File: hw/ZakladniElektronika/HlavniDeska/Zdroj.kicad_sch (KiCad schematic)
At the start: 28 parts, among them Q10 Q_PMOS_DGS-L, SW1 ON, U17 BateriCell_2x, U7 SL8261D-G3JE

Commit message: AHS-V1
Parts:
- Q10, Q? (x2), U7: JLCPCB_CORRECTION (none) -> 0;0;180
- Q? (x3): JLCPCB_CORRECTION (none) -> 0;0;-90
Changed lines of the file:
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@@
       (effects (font (size 1.27 1.27)) hide)
     )
-    (property "JLCPCB_CORRECTION" "" (at 190.5 88.9 0)
+    (property "JLCPCB_CORRECTION" "0;0;-90" (at 190.5 88.9 0)
       (effects (font (size 1.27 1.27)) hide)
     )
@@
       (effects (font (size 1.27 1.27)) hide)
     )
-    (property "JLCPCB_CORRECTION" "" (at 91.44 129.54 0)
+    (property "JLCPCB_CORRECTION" "0;0;180" (at 91.44 129.54 0)
       (effects (font (size 1.27 1.27)) hide)
     )
@@
       (effects (font (size 1.27 1.27)) hide)
     )
-    (property "JLCPCB_CORRECTION" "" (at 142.24 129.54 0)
+    (property "JLCPCB_CORRECTION" "0;0;180" (at 142.24 129.54 0)
       (effects (font (size 1.27 1.27)) hide)
     )
@@
       (effects (font (size 1.27 1.27)) hide)
     )
-    (property "JLCPCB_CORRECTION" "" (at 109.22 88.9 0)
+    (property "JLCPCB_CORRECTION" "0;0;-90" (at 109.22 88.9 0)
       (effects (font (size 1.27 1.27)) hide)
     )
@@
     )
     (property "LCSC" "C5186027" (at 179.07 58.42 0)
+      (effects (font (size 1.27 1.27)) hide)
+    )
+    (property "JLCPCB_CORRECTION" "0;0;180" (at 179.07 73.66 0)
       (effects (font (size 1.27 1.27)) hide)
     )
@@
       (effects (font (size 1.27 1.27)) hide)
     )
-    (property "JLCPCB_CORRECTION" "" (at 157.48 66.04 0)
+    (property "JLCPCB_CORRECTION" "0;0;180" (at 157.48 66.04 0)
       (effects (font (size 1.27 1.27)) hide)
     )
@@
       (effects (font (size 1.27 1.27)) hide)
     )
-    (property "JLCPCB_CORRECTION" "" (at 208.28 88.9 0)
-      (effects (font (size 1.27 1.27)) hide)
-    )
+    (property "JLCPCB_CORRECTION" "0;0;-90" (at 208.28 88.9 0)
+      (effects (font (size 1.27 1.27)) hide)
+    )

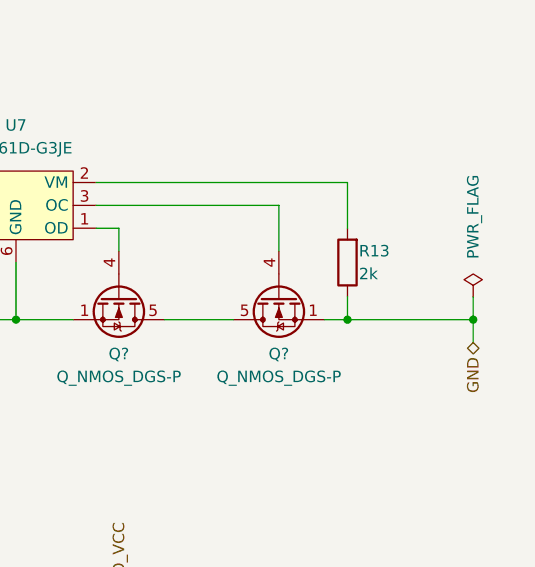
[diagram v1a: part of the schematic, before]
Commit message: Řešení issue "Držák baterek" a " SemiSemafor V0"
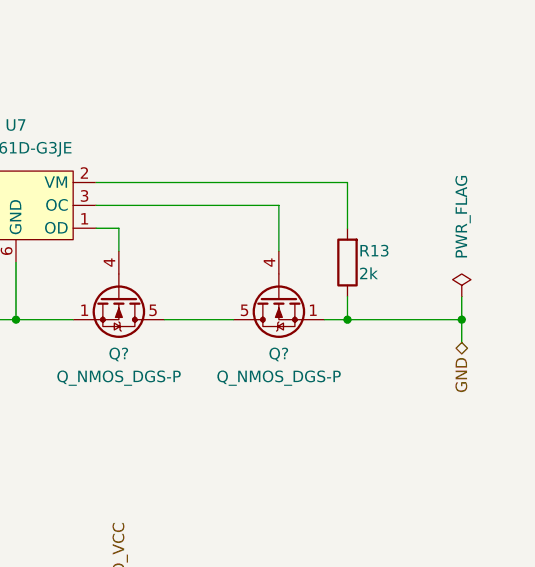
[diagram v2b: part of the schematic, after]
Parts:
- U17: footprint RKL-Batteries:battery_dock -> RKL-Batteries:2x18650-holder-jlc_SMD-typ; JLCPCB_IGNORE ignore -> (none); LCSC (none) -> C6937126
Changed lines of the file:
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@@
   (junction (at 88.9 88.9) (diameter 0) (color 0 0 0 0)
   )
-  (junction (at 229.87 88.9) (diameter 0) (color 0 0 0 0)
+  (junction (at 228.6 88.9) (diameter 0) (color 0 0 0 0)
   )
   (junction (at 160.02 50.8) (diameter 0) (color 0 0 0 0)
@@
     (stroke (width 0) (type default))
   )
-  (wire (pts (xy 215.9 88.9) (xy 229.87 88.9))
-    (stroke (width 0) (type default))
-  )
   (wire (pts (xy 203.2 88.9) (xy 195.58 88.9))
     (stroke (width 0) (type default))
@@
     (stroke (width 0) (type default))
   )
-  (wire (pts (xy 215.9 88.9) (xy 213.36 88.9))
+  (wire (pts (xy 213.36 88.9) (xy 215.9 88.9))
     (stroke (width 0) (type default))
   )
@@
     (stroke (width 0) (type default))
   )
-  (wire (pts (xy 229.87 86.36) (xy 229.87 88.9))
+  (wire (pts (xy 228.6 86.36) (xy 228.6 88.9))
     (stroke (width 0) (type default))
   )
@@
     (stroke (width 0) (type default))
   )
-  (wire (pts (xy 229.87 91.44) (xy 229.87 88.9))
+  (wire (pts (xy 228.6 91.44) (xy 228.6 88.9))
     (stroke (width 0) (type default))
   )
@@
   )
   (wire (pts (xy 88.9 139.7) (xy 88.9 134.62))
+    (stroke (width 0) (type default))
+  )
+  (wire (pts (xy 215.9 88.9) (xy 228.6 88.9))
     (stroke (width 0) (type default))
   )
@@
     (effects (font (size 1.27 1.27)) (justify left bottom))
   )
-  (hierarchical_label "GND" (shape bidirectional) (at 229.87 91.44 270) (fields_autoplaced)
+  (hierarchical_label "GND" (shape bidirectional) (at 228.6 91.44 270) (fields_autoplaced)
     (effects (font (size 1.27 1.27)) (justify right))
   )
@@
     )
   )
-  (symbol (lib_id "power:PWR_FLAG") (at 229.87 86.36 0) (unit 1)
-    (in_bom yes) (on_board yes) (dnp no)
-    (property "Reference" "#FLG02" (at 229.87 84.455 0)
-      (effects (font (size 1.27 1.27)) hide)
-    )
-    (property "Value" "PWR_FLAG" (at 229.87 77.47 90)
+  (symbol (lib_id "power:PWR_FLAG") (at 228.6 86.36 0) (unit 1)
+    (in_bom yes) (on_board yes) (dnp no)
+    (property "Reference" "#FLG02" (at 228.6 84.455 0)
+      (effects (font (size 1.27 1.27)) hide)
+    )
+    (property "Value" "PWR_FLAG" (at 228.6 77.47 90)
       (effects (font (size 1.27 1.27)))
     )
-    (property "Footprint" "" (at 229.87 86.36 0)
-      (effects (font (size 1.27 1.27)) hide)
-    )
-    (property "Datasheet" "~" (at 229.87 86.36 0)
+    (property "Footprint" "" (at 228.6 86.36 0)
+      (effects (font (size 1.27 1.27)) hide)
+    )
+    (property "Datasheet" "~" (at 228.6 86.36 0)
       (effects (font (size 1.27 1.27)) hide)
     )
@@
       (effects (font (size 1.27 1.27)) (justify left))
     )
-    (property "Footprint" "RKL-Batteries:battery_dock" (at 86.36 80.01 0)
-      (effects (font (size 1.27 1.27)) hide)
-    )
-    (property "Datasheet" "" (at 86.36 80.01 0)
-      (effects (font (size 1.27 1.27)) hide)
-    )
-    (property "JLCPCB_IGNORE" "ignore" (at 86.36 80.01 0)
-      (effects (font (size 1.27 1.27)) hide)
-    )
+    (property "Footprint" "RKL-Batteries:2x18650-holder-jlc_SMD-typ" (at 86.36 80.01 0)
+      (effects (font (size 1.27 1.27)) hide)
+    )
+    (property "Datasheet" "https://wmsc.lcsc.com/wmsc/upload/file/pdf/v2/lcsc/2306250925_MYOUNG-BH-18650-B1BA007_C6937126.pdf" (at 86.36 80.01 0)
+      (effects (font (size 1.27 1.27)) hide)
+    )
+    (property "LCSC" "C6937126" (at 86.36 80.01 0)
+      (effects (font (size 1.27 1.27)) hide)
+    )

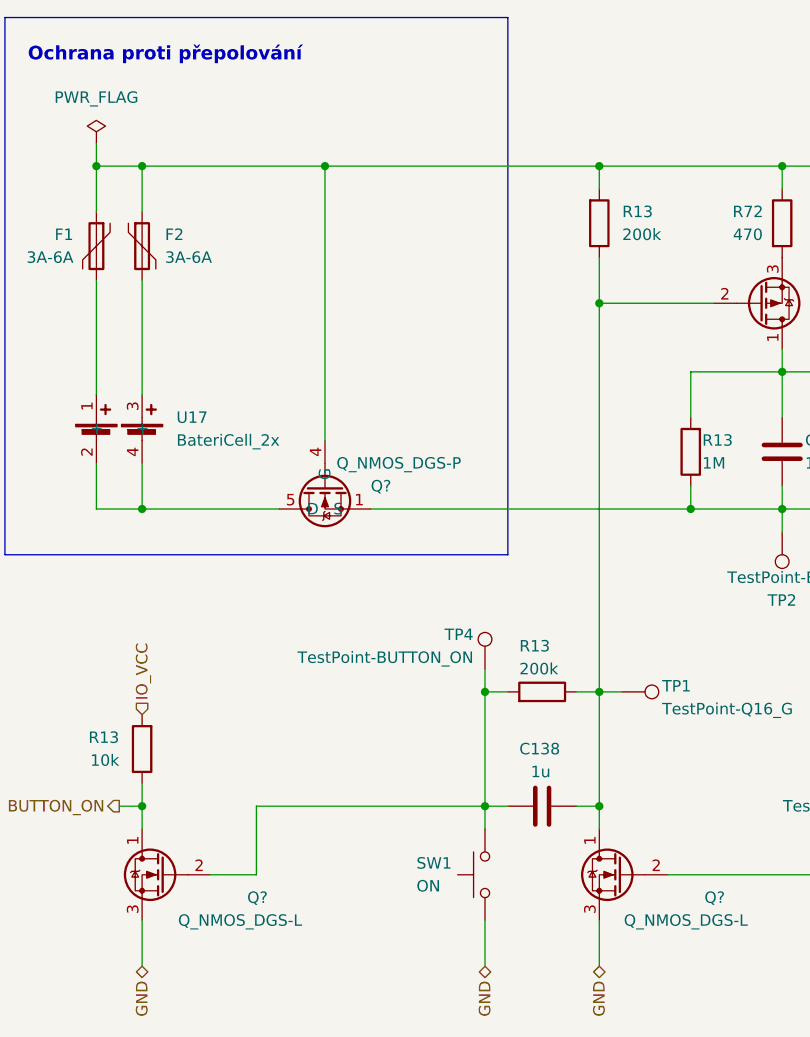
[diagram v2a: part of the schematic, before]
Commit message: Řešení issue "Čtení zapínacího tlačítka"
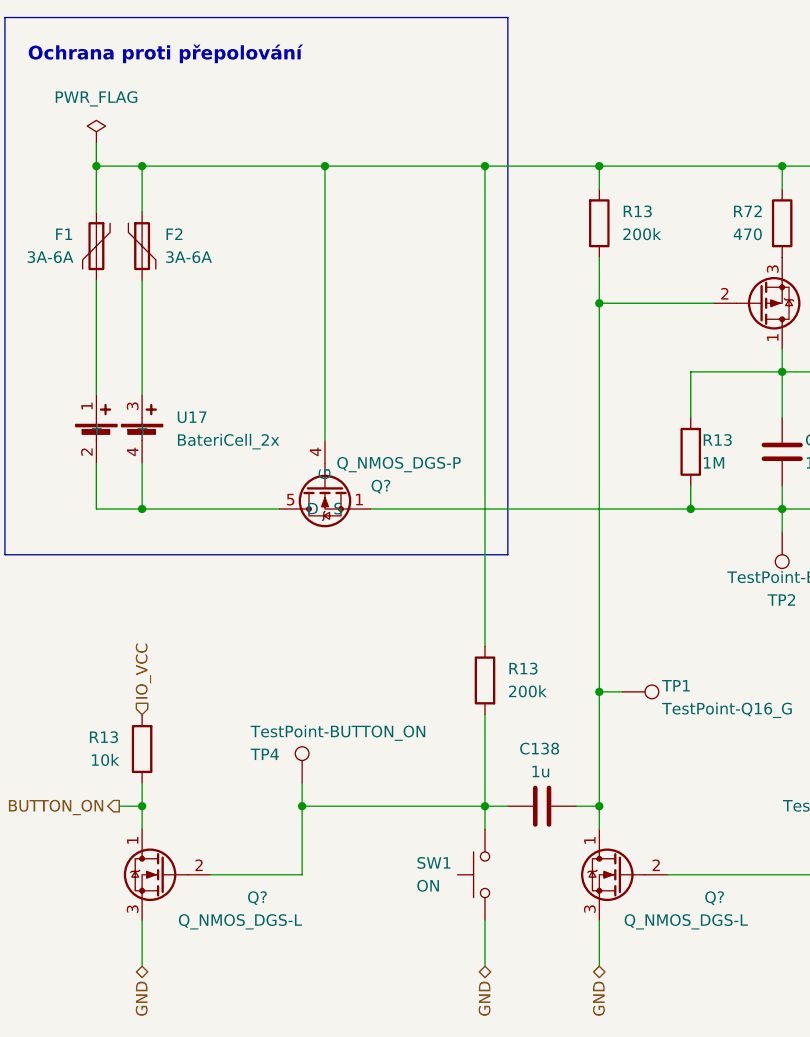
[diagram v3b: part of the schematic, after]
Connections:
- net VCC: now also R13.1
- net at C138.1, Q10.2 (G), Q?.1 (D)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: no longer R13.1
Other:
- moved on the sheet: R13, TP4
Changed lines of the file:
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@@
   (junction (at 160.02 88.9) (diameter 0) (color 0 0 0 0)
   )
-  (junction (at 127 109.22) (diameter 0) (color 0 0 0 0)
-  )
   (junction (at 88.9 88.9) (diameter 0) (color 0 0 0 0)
   )
@@
   (junction (at 160.02 50.8) (diameter 0) (color 0 0 0 0)
   )
+  (junction (at 106.68 121.92) (diameter 0) (color 0 0 0 0)
+  )
   (junction (at 83.82 50.8) (diameter 0) (color 0 0 0 0)
   )
@@
   )
   (junction (at 109.22 50.8) (diameter 0) (color 0 0 0 0)
+  )
+  (junction (at 127 50.8) (diameter 0) (color 0 0 0 0)
   )
   (junction (at 190.5 129.54) (diameter 0) (color 0 0 0 0)
@@
     (stroke (width 0) (type default))
   )
-  (wire (pts (xy 137.16 109.22) (xy 139.7 109.22))
-    (stroke (width 0) (type default))
-  )
-  (wire (pts (xy 127 106.68) (xy 127 109.22))
-    (stroke (width 0) (type default))
-  )
-  (wire (pts (xy 101.6 121.92) (xy 127 121.92))
+  (wire (pts (xy 106.68 119.38) (xy 106.68 121.92))
+    (stroke (width 0) (type default))
+  )
+  (wire (pts (xy 106.68 121.92) (xy 127 121.92))
     (stroke (width 0) (type default))
   )
@@
     (stroke (width 0) (type default))
   )
-  (wire (pts (xy 109.22 50.8) (xy 139.7 50.8))
+  (wire (pts (xy 109.22 50.8) (xy 127 50.8))
     (stroke (width 0) (type default))
   )
@@
     (stroke (width 0) (type default))
   )
+  (wire (pts (xy 127 50.8) (xy 127 104.14))
+    (stroke (width 0) (type default))
+  )
   (wire (pts (xy 203.2 88.9) (xy 195.58 88.9))
     (stroke (width 0) (type default))
@@
     (stroke (width 0) (type default))
   )
+  (wire (pts (xy 127 111.76) (xy 127 121.92))
+    (stroke (width 0) (type default))
+  )
   (wire (pts (xy 114.3 88.9) (xy 149.86 88.9))
     (stroke (width 0) (type default))
@@
     (stroke (width 0) (type default))
   )
-  (wire (pts (xy 96.52 129.54) (xy 101.6 129.54))
+  (wire (pts (xy 96.52 129.54) (xy 106.68 129.54))
     (stroke (width 0) (type default))
   )
@@
     (stroke (width 0) (type default))
   )
-  (wire (pts (xy 127 109.22) (xy 127 121.92))
-    (stroke (width 0) (type default))
-  )
   (wire (pts (xy 215.9 48.26) (xy 215.9 50.8))
     (stroke (width 0) (type default))
@@
     (stroke (width 0) (type default))
   )
-  (wire (pts (xy 127 109.22) (xy 129.54 109.22))
-    (stroke (width 0) (type default))
-  )
   (wire (pts (xy 177.8 129.54) (xy 177.8 132.08))
     (stroke (width 0) (type default))
@@
     (stroke (width 0) (type default))
   )
-  (wire (pts (xy 101.6 121.92) (xy 101.6 129.54))
+  (wire (pts (xy 106.68 121.92) (xy 106.68 129.54))
     (stroke (width 0) (type default))
   )
@@
   )
   (wire (pts (xy 228.6 86.36) (xy 228.6 88.9))
+    (stroke (width 0) (type default))
+  )
+  (wire (pts (xy 127 50.8) (xy 139.7 50.8))
     (stroke (width 0) (type default))
   )
@@
     )
   )
-  (symbol (lib_id "Device:R") (at 133.35 109.22 270) (mirror x) (unit 1)
-    (in_bom yes) (on_board yes) (dnp no)
-    (property "Reference" "R13" (at 130.81 104.14 90)
-      (effects (font (size 1.27 1.27)) (justify left))
-    )
-    (property "Value" "200k" (at 130.81 106.68 90)
-      (effects (font (size 1.27 1.27)) (justify left))
-    )
-    (property "Footprint" "Resistor_SMD:R_0402_1005Metric" (at 133.35 110.998 90)
-      (effects (font (size 1.27 1.27)) hide)
-    )
-    (property "Datasheet" "~" (at 133.35 109.22 0)
-      (effects (font (size 1.27 1.27)) hide)
-    )
-    (property "LCSC" "C25764" (at 133.35 109.22 0)
-      (effects (font (size 1.27 1.27)) hide)
-    )
-    (property "Basic/Extended" "B" (at 133.35 109.22 0)
+  (symbol (lib_id "Device:R") (at 127 107.95 0) (mirror y) (unit 1)
+    (in_bom yes) (on_board yes) (dnp no)
+    (property "Reference" "R13" (at 129.54 106.68 0)
+      (effects (font (size 1.27 1.27)) (justify right))
+    )
+    (property "Value" "200k" (at 129.54 109.22 0)
+      (effects (font (size 1.27 1.27)) (justify right))
+    )
+    (property "Footprint" "Resistor_SMD:R_0402_1005Metric" (at 128.778 107.95 90)
+      (effects (font (size 1.27 1.27)) hide)
+    )
+    (property "Datasheet" "~" (at 127 107.95 0)
+      (effects (font (size 1.27 1.27)) hide)
+    )
+    (property "LCSC" "C25764" (at 127 107.95 0)
+      (effects (font (size 1.27 1.27)) hide)
+    )
+    (property "Basic/Extended" "B" (at 127 107.95 0)
       (effects (font (size 1.27 1.27)) hide)
     )
@@
     )
   )
-  (symbol (lib_id "Connector:TestPoint") (at 127 106.68 0) (unit 1)
-    (in_bom yes) (on_board yes) (dnp no)
-    (property "Reference" "TP4" (at 125.73 102.87 0)
-      (effects (font (size 1.27 1.27)) (justify right))
-    )
-    (property "Value" "TestPoint-BUTTON_ON" (at 125.73 105.41 0)
-      (effects (font (size 1.27 1.27)) (justify right))
-    )
-    (property "Footprint" "Connector_Pin:Pin_D0.9mm_L10.0mm_W2.4mm_FlatFork" (at 132.08 106.68 0)
-      (effects (font (size 1.27 1.27)) hide)
-    )
-    (property "Datasheet" "~" (at 132.08 106.68 0)
-      (effects (font (size 1.27 1.27)) hide)
-    )
-    (property "JLCPCB_IGNORE" "ignore" (at 127 106.68 0)
-      (effects (font (size 1.27 1.27)) hide)
-    )
+  (symbol (lib_id "Connector:TestPoint") (at 106.68 119.38 0) (unit 1)
+    (in_bom yes) (on_board yes) (dnp no)
+    (property "Reference" "TP4" (at 100.965 116.205 0)
+      (effects (font (size 1.27 1.27)) (justify left))
+    )
+    (property "Value" "TestPoint-BUTTON_ON" (at 100.965 113.665 0)
+      (effects (font (size 1.27 1.27)) (justify left))
+    )
+    (property "Footprint" "Connector_Pin:Pin_D0.9mm_L10.0mm_W2.4mm_FlatFork" (at 111.76 119.38 0)
+      (effects (font (size 1.27 1.27)) hide)
+    )
+    (property "Datasheet" "~" (at 111.76 119.38 0)
+      (effects (font (size 1.27 1.27)) hide)
+    )
+    (property "JLCPCB_IGNORE" "ignore" (at 106.68 119.38 0)
+      (effects (font (size 1.27 1.27)) hide)
+    )

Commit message: WPI (zápínací logika)
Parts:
- removed C138: 1u, Capacitor_SMD:C_0402_1005Metric, symbol Device:C
- removed Q10: Q_PMOS_DGS-L, Package_TO_SOT_SMD:SOT-23, symbol Device:Q_PMOS_DGS
- removed Q?: Q_NMOS_DGS-L, Package_TO_SOT_SMD:SOT-23, symbol Device:Q_NMOS_DGS
- removed R13: 1M, Resistor_SMD:R_0402_1005Metric, symbol Device:R
- removed R13 (x2): 200k, Resistor_SMD:R_0402_1005Metric, symbol Device:R
- removed TP1: TestPoint-Q16_G, Connector_Pin:Pin_D0.9mm_L10.0mm_W2.4mm_FlatFork, symbol Connector:TestPoint
- removed TP4: TestPoint-BUTTON_ON, Connector_Pin:Pin_D0.9mm_L10.0mm_W2.4mm_FlatFork, symbol Connector:TestPoint
- removed TP5: TestPoint-EN_ALL, Connector_Pin:Pin_D0.9mm_L10.0mm_W2.4mm_FlatFork, symbol Connector:TestPoint
- added Q?: Q_NMOS_DGS-P, Package_SON:Diodes_PowerDI3333-8, symbol RKL-Uncategorized:Si7112DN
- added Q?: Q_NMOS_DGS-L, Package_TO_SOT_SMD:SOT-23, symbol Device:Q_NMOS_DGS
- added R13: 10k, Resistor_SMD:R_0402_1005Metric, symbol Device:R
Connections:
- net GND: now also Q?.1 (S), Q?.2 (S), Q?.3 (S), R13.1; no longer Q?.1 (S), Q?.2 (S), Q?.3 (S), R13.1, SW1.1
- net VCC: now also SW1.1, Q?.1 (D)
- net at Q?.2 (G), SW1.2: now also Q?.2 (G), R13.2
- net at C138.1, R13.1, R13.2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: now also Q?.3 (S), Q?.4 (G)
- net at C18.1, U7.5 (VCC): now also R72.2
- new net: Q?.1 (S), Q?.2 (S), Q?.3 (S), Q?.5 (D), R13.1
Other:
- moved on the sheet: C138, C18, F1, F2, Q?, R13, R23, R72, SW1, TP2, TP3, U17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

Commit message: KiCad V8
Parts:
- renumbered C18 to C143, C138 to C163, F1 to F3, F2 to F4, R13 to R33, R72 to R35, R13 to R36, R13 to R67, R13 to R68, R23 to R69, R13 to R70, SW1 to SW3
